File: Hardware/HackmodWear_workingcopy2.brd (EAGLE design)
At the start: 99.9 x 104.8 mm, 133 parts, among them Q1 ZXMP6A13F, U1 ATSAMD21G-A, U2 3.3V, U5 OPA344, U6 ADMP401, U7 APDS-9960, Y1 32.768kHz

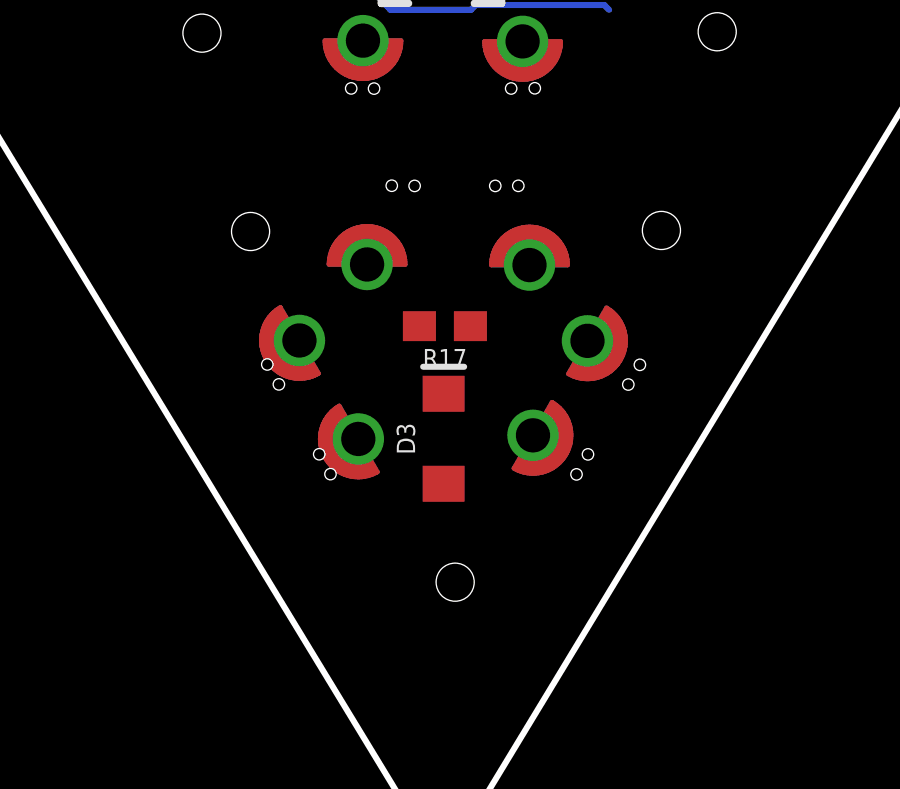
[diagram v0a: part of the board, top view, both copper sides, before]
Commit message: Moving bottom triangle in line with the outer dimension
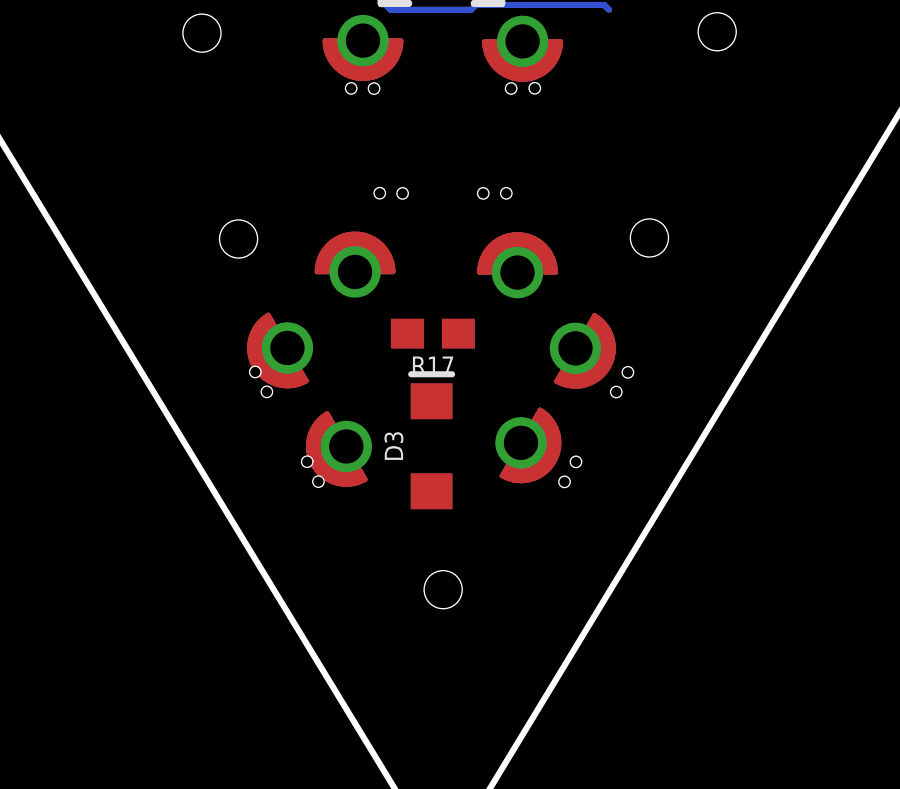
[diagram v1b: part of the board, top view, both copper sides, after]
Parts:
- moved J65 0.47 mm to (47.7, 20.6)
- moved J69 0.47 mm to (55.1, 18.1)
- moved D3 0.47 mm to (50.3, 14.8)
- moved J66 0.47 mm to (53.3, 14.9)
- moved J67 0.47 mm to (45.5, 18.1)
- moved J68 0.47 mm to (47.4, 14.8)
- moved J70 0.47 mm to (53.1, 20.6)
- moved R17 0.47 mm to (50.3, 18.6)
